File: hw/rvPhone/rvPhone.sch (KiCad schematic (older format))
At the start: 119 parts, among them J1 USB_OTG, J2 BATT, J3 SJ-3571N, Q1 MMBT3906, SW1 RESET, SW2 WAKE, U1 BQ25895, U10 74HC595, U11 ICS-43434, U12 MAX98357A, U13 FT813Q, U14 FAN5333BSX, U2 TPS62293, U3 TPS630250, U4 TMUX154E, U5 E310-G002, U6 IS25LP128-JBLE, U7 74HC00, U8 74HC00, U9 74HC595, X1 SiT1533, Y1 16MHz, Y2 12MHz

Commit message: stereo audio out; lvds display; LSM9DS1 added
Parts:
- removed BZ1: Buzzer, footprints:Buzzer_12x9.5RM5.0, symbol Device:Buzzer
- removed C38, C39: 18pF, Capacitor_SMD:C_0603_1608Metric, symbol Device:C_Small
- removed C40, C41, C43, C45, C47: 0.1uF, Capacitor_SMD:C_0603_1608Metric, symbol Device:C_Small
- removed C42, C44: 27pF, Capacitor_SMD:C_0603_1608Metric, symbol Device:C_Small
- removed C46: 4.7uF, Capacitor_SMD:C_0603_1608Metric, symbol Device:C_Small
- removed C48, C49: 1uF, Capacitor_SMD:C_0603_1608Metric, symbol Device:C
- removed C50: 10uF, Capacitor_SMD:C_0603_1608Metric, symbol Device:C
- removed C51, C53: 27pF, Capacitor_SMD:C_0603_1608Metric, symbol Device:C
- removed C52, C54: 0.1uF, Capacitor_SMD:C_0603_1608Metric, symbol Device:C
- removed D2: MBR0540, Diode_SMD:D_SOD-123, symbol Device:D_Schottky
- removed D3: 3SMAJ5935B-TP, Diode_SMD:D_SMA, symbol Device:D_Zener
- removed J3: SJ-3571N, footprints:CUI_SJ-3571N, symbol cui-sj:SJ-3571N
- removed L4: 10uH, footprints:L_Murata_LQH66SN, symbol Device:L
- removed Q1: MMBT3906, Package_TO_SOT_SMD:SOT-23, symbol Transistor_BJT:MMBT3906
- removed R28, R29: 47K, Resistor_SMD:R_0603_1608Metric, symbol Device:R
- removed U1: BQ25895, Package_DFN_QFN:Texas_S-PWQFN-N24_EP2.7x2.7mm_ThermalVias, symbol texas-tps:BQ25895
- removed U11: ICS-43434, footprints:TDK_ICS-43434, symbol ics-43434:ICS-43434
- removed U12: MAX98357A, footprints:TQFN-16-1EP_3x3mm_P0.5mm_EP1.23x1.23mm_ThermalVias, symbol max98357:MAX98357
- removed U13: FT813Q, Package_DFN_QFN:QFN-56-1EP_8x8mm_P0.5mm_EP5.6x5.6mm_ThermalVias, symbol ft81x:FT813Q
- removed U14: FAN5333BSX, Package_TO_SOT_SMD:SOT-23-5, symbol fan5333:FAN5333
- removed U2: TPS62293, footprints:TPS62290, symbol texas-tps:TPS62290
- removed U3: TPS630250, footprints:TPS630250, symbol texas-tps:TPS630250
- removed U4: TMUX154E, Package_DFN_QFN:UQFN-10_1.3x1.8mm_P0.4mm, symbol tmux:TMUX154E
- removed U5: E310-G002, Package_DFN_QFN:QFN-48-1EP_6x6mm_P0.4mm_EP4.2x4.2mm_ThermalVias, symbol e310-g000:E310-G002
- removed U6: IS25LP128-JBLE, Package_SO:SOIJ-8_5.3x5.3mm_P1.27mm, symbol is25lp128:IS25LP128
- removed X1: SiT1533, footprints:SiT1533, symbol sit1533:SiT1533
- removed Y2: 12MHz, footprints:TXC_7M, symbol Device:Crystal_GND3_Small
- added C38, C39: 10uF, Capacitor_SMD:C_0603_1608Metric, symbol Device:C
- added C40, C41: 0.1uF, Capacitor_SMD:C_0603_1608Metric, symbol Device:C
- added J3: SJ-3571N, footprints:SJ-3571N, symbol cui:SJ-3571N
- added LS2: Speaker, Connector_PinHeader_1.27mm:PinHeader_1x02_P1.27mm_Vertical, symbol Device:Speaker
- added U1: BQ25895, Package_DFN_QFN:Texas_S-PWQFN-N24_EP2.7x2.7mm_ThermalVias, symbol bq:BQ25895
- added U11: ICS-43434, footprints:ICS-43434, symbol ics:ICS-43434
- added U12, U13: MAX98357A, footprints:TQFN-16-1EP_3x3mm_P0.5mm_EP1.23x1.23mm_ThermalVias, symbol max:MAX98357
- added U14: SN74LVC1G04DRY, footprints:USON-6_1.45x1mm_P0.5mm, symbol sn74:SN74LVC1G04DRY
- added U15: SN74LVC1G3157DRY, footprints:USON-6_1.45x1mm_P0.5mm, symbol sn74:SN74LVC1G3157DRY
- added U2: TPS62293, footprints:TPS62290, symbol tps:TPS62293
- added U3: TPS630250, footprints:TPS630250, symbol tps:TPS630250
- added U4: E310-G002, Package_DFN_QFN:QFN-48-1EP_6x6mm_P0.4mm_EP4.2x4.2mm_ThermalVias, symbol sifive:E310-G002
- added U5: IS25LP128-JKLE, Package_SON:WSON-8-1EP_6x5mm_P1.27mm_EP3.4x4mm, symbol issi:IS25LP128-JKLE
- added U6: TMUX1574RSV, footprints:UQFN-16_1.8x2.6mm_P0.4mm, symbol tmux:TMUX1574RSV
- added X1: SiT1533, footprints:SiT1533, symbol sit:SiT1533
- C36: value 220pF -> 0.1uF
- C37: value 220pF -> 10uF
- R15, R16: value 1K -> 100K
- R23: value 47K -> 2K
- R24: value 22R -> 210K
- R25: value 15R -> 47K
- R26: value R -> 47K
- R27: value 47K -> 100K
- renumbered C16 to C15, C17 to C16, C18 to C17, C19 to C18, C20 to C19, C21 to C20, C22 to C21, C23 to C22, C25 to C23, C26 to C24, C27 to C25, C28 to C26, C24 to C27, C15 to C28, C35 to C34, C34 to C35, R5 to R13, R6 to R14, R13 to R28, R14 to R29, R8 to R5, R9 to R6, R35 to R8, R36 to R9
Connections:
- net BL_PWM is gone; now on net SPK_EN: R23.2
- net SPK_VO+ is gone; now on net +VSYS: C37.1
- net +1V8: now also U2.3 (FB), U4.30 (VDD), U4.46 (VDD), U4.6 (VDD)
- net +3V3: now also R27.2, C40.1, U11.5 (VDD), U14.6 (VCC), U3.12 (VOUT), U3.13 (VOUT), U3.14 (VOUT), U4.11 (IVDD), U4.12 (OTP_AIVDD), U4.19 (AON_IVDD), U4.23 (AON_VDD), U4.32 (IVDD), U4.47 (IVDD), U5.8 (VCC), U6.14 (VCC), X1.4 (VCC); no longer C34.1, C35.1, R27.1, R28.1
- net +VSYS: now also C34.1, C35.1, C36.1, R28.1, C41.1, U1.15 (SYS), U1.16 (SYS), U12.7 (VDD), U12.8 (VDD), U13.7 (VDD), U13.8 (VDD), U15.5 (VCC), U2.4 (EN), U2.5 (VIN), U3.4 (VIN), U3.5 (VIN), U3.6 (VIN), U3.7 (VINA), U3.8 (EN); no longer R23.1
- net ESP32.IO39: now also U1.7 (INT)
- net GND: now also R15.2, Y1.3, C40.2, C41.2, J3.1, U1.17 (PGND), U1.18 (PGND), U1.25 (EP), U1.8 (OTG), U1.9 (/CE), U11.2 (LR), U11.3 (GND), U12.11 (GND), U12.15 (GND), U12.17 (EP), U12.3 (GND), U13.11 (GND), U13.15 (GND), U13.17 (EP), U13.3 (GND), U14.3 (GND), U15.2 (GND), U2.2 (MODE), U2.6 (GND), U2.7 (EP), U3.10 (PFM), U3.2 (PGND), U3.9 (GND), U4.21 (AON_PSD_LFCLKSEL), U4.49 (GND), U5.4 (VSS), U5.9 (EP), U6.13 (/EN), U6.6 (GND), X1.2 (GND); no longer R24.2, U8.12, U8.13
- net GPIO_0: now also U4.25 (GPIO_0/PWM0.0)
- net GPIO_12: now also U4.36 (GPIO_12/PWM2.2), U6.7 (D3)
- net GPIO_13: now also U4.37 (GPIO_13/PWM2.3), U6.5 (D2)
- net GPIO_18: now also U4.40 (GPIO_18)
- net GPIO_20: now also U4.42 (GPIO_20/PWM1.0)
- net GPIO_22: now also U4.44 (GPIO_22/PWM1.3)
- net GPIO_23: now also U4.45 (GPIO_23)
- net JTAG_TCK: now also U4.13 (JTAG_TCK)
- net JTAG_TDI: now also U4.16 (JTAG_TDI)
- net JTAG_TDO: now also U4.14 (JTAG_TDO)
- net JTAG_TMS: now also U4.15 (JTAG_TMS)
- net PLL_AVDD: now also U4.7 (PLL_AVDD)
- net PLL_AVSS: now also U4.8 (PLL_AVSS)
- net PSD_LFALTCLK: now also U4.20 (AON_PSD_LFALTCLK), X1.3 (CLKOUT)
- net PWM0.1: now also U4.26 (GPIO_1/PWM0.1), U6.10 (D4); no longer R18.2, U7.1, U8.1, U8.2
- net PWM1.1: now also U4.41 (GPIO_19/PWM1.1), U6.2 (D1); no longer R19.2
- net PWM1.2: now also U4.43 (GPIO_21/PWM1.2)
- net PWM2.1: now also U8.1, U12.14 (LRCLK), U13.14 (LRCLK), U4.35 (GPIO_11/PWM2.1); no longer U8.10
- net QSPI_CLK: now also U4.48 (QSPI_CLK), U5.6 (SCK)
- net QSPI_CS: now also U4.5 (QSPI_CS), U5.1 (S#)
- net QSPI_DQ_0: now also U4.4 (QSPI_DQ_0), U5.5 (MOSI/IO0)
- net QSPI_DQ_1: now also U4.3 (QSPI_DQ_1), U5.2 (MISO/IO1)
- net QSPI_DQ_2: now also U4.2 (QSPI_DQ_2), U5.3 (WP#/IO2)
- net QSPI_DQ_3: now also U4.1 (QSPI_DQ_3), U5.7 (HOLD#/IO3)
- net RESET: now also U4.24 (AON_ERST_N)
- net SPI1.MISO: now also U4.29 (GPIO_4/SPI1.MISO)
- net SPI1.MOSI: now also U4.28 (GPIO_3/SPI1.MOSI/PWM0.3)
- net SPI1.SCK: now also U4.31 (GPIO_5/SPI1.SCK)
- net SPI1.SS0: now also U4.27 (GPIO_2/SPI1.SS0/PWM0.2)
- net SPI1.SS2: now also U4.33 (GPIO_9/SPI1.SS2); no longer R27.2
- net SPI1.SS3: now also U4.34 (GPIO_10/SPI1.SS3/PWM2.0)
- net SPK_CLK: now also U8.11, U12.16 (BCLK), U13.16 (BCLK); no longer U8.3
- net SPK_EN: now also R24.2, U6.15 (SEL)
- net SPK_GAIN: now also U12.2 (GAIN_SLOT), U13.2 (GAIN_SLOT), U15.4 (A)
- net TMUX.I2C0.SCL: now also U1.5 (SCL), U6.3 (S2A)
- net TMUX.I2C0.SDA: now also U1.6 (SDA), U6.9 (S3A)
- net UART0.RX: now also U4.38 (GPIO_16/UART0.RX)
- net UART0.TX: now also U4.39 (GPIO_17/UART0.TX)
- net VBUS: now also U1.1 (VBUS)
- net WAKE: now also U1.12 (/QON), U4.18 (AON_PMU_DWAKEUP_N)
- net XTAL_XI: now also U4.9 (16M_XTAL_XI)
- net XTAL_XO: now also U4.10 (16M_XTAL_XO)
- net at L2.1: now also U2.1 (SW)
- net TMUX.GPIO0: now reaches R15.1
- net TMUX.GPIO0: now also U6.16 (S1A)
- net SPK_GAIN_SEL: now reaches U8.8
- net SPK_GAIN_SEL: now also U15.6 (S); no longer R15.2
- net TMUX.GPIO1: now reaches R16.1
- net TMUX.GPIO1: now also U6.12 (S4A)
- net at R1.1: now also U1.10 (ILIM)
- net at R2.2, R4.1: now also U1.11 (TS)
- net at C6.1, J2.1 (Pin_1): now also U1.13 (BAT), U1.14 (BAT)
- net at C1.1, L1.1: now also U1.19 (SW), U1.20 (SW)
- net at J1.3 (D+): now also U1.2 (D+)
- net at C1.2: now also U1.21 (BTST)
- net at C5.1, R2.1: now also U1.22 (REGN)
- net at C55.1, C56.1: now also U1.23 (PMID)
- net at J1.2 (D-): now also U1.3 (D-)
- net at R3.1: now also U1.4 (STAT)
- net at L3.1: now also U3.3 (L1)
- net at L3.2: now also U3.1 (L2)
- net at R29.1: now also U15.3 (B1)
- net at R28.2: now also U15.1 (B2)
- net at R5.2, R6.1: now also U3.11 (FB)
- net at U8.6: now also U8.2; no longer U8.9
- removed net DISP_LED_K: R24.1, R25.1, R26.1
- net EAR_VO+ renamed SPK_L+
- net SPK_L+: now also J3.4
- net I2S_SD_IN renamed SPK_SD
- net SPK_SD: now also U12.1 (DIN), U13.1 (DIN), U6.4 (S2B)
- net I2S_SD_OUT renamed MIC_SD
- net MIC_SD: now also U11.6 (SD), U6.8 (S3B)
- net SPK_VO- renamed SPK_L-
- net SPK_L-: now also U12.10 (OUTN); no longer C36.1
- new net: R23.1, U12.4 (SD_MODE)
- new net: R24.1, U13.4 (SD_MODE)
- new net: C39.1, J3.2, R26.1
- new net: C39.2, J3.6
- new net: C38.1, J3.3, R25.1
- new net: C38.2, J3.9
- new net BT81X.GPIO2: U8.10
- new net DISP_CS: U8.3
- new net HP_DET: J3.10, J3.11, R27.1, U14.2 (A)
- new net HP_SWITCH: U14.4 (Y), U8.9
- new net MIC_CLK: R18.2, U11.4 (SCK), U6.11 (S4B), U7.1, U8.12, U8.13
- new net MIC_WS: R19.2, U11.1 (WS), U6.1 (S1B)
- new net SPK_L_HP+: J3.5, U12.9 (OUTP)
- new net SPK_R+: J3.7, LS2.1
- new net SPK_R-: LS2.2, U13.10 (OUTN)
- new net SPK_R_HP_+: J3.8, U13.9 (OUTP)
- no-connect marks 26 -> 21
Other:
- moved on the sheet: C1, C10, C11, C12, C13, C14, C15, C16, C17, C18, C19, C2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

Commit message: rev2 board
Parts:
- removed LS1, LS2: Speaker, Connector_PinHeader_1.27mm:PinHeader_1x02_P1.27mm_Vertical, symbol Device:Speaker
- removed U14: SN74LVC1G04DRY, footprints:USON-6_1.45x1mm_P0.5mm, symbol sn74:SN74LVC1G04DRY
- removed U15: SN74LVC1G3157DRY, footprints:USON-6_1.45x1mm_P0.5mm, symbol sn74:SN74LVC1G3157DRY
- removed U4: E310-G002, Package_DFN_QFN:QFN-48-1EP_6x6mm_P0.4mm_EP4.2x4.2mm_ThermalVias, symbol sifive:E310-G002
- added C42: 10uF, Capacitor_SMD:C_0603_1608Metric, symbol Device:C
- added C45: 0.1uF, Capacitor_SMD:C_0603_1608Metric, symbol Device:C_Small
- added J3: +5V, Connector_PinHeader_2.54mm:PinHeader_1x02_P2.54mm_Vertical, symbol Connector_Generic:Conn_01x02
- added J5: SPEAKER, Connector_PinHeader_2.54mm:PinHeader_1x04_P2.54mm_Vertical, symbol Connector_Generic:Conn_01x04
- added TP1: BQ_INT, TestPoint:TestPoint_Pad_D1.5mm, symbol Connector:TestPoint
- added U14: SN74LVC1G04DCK, footprints:Texas_R-PDSO-G5, symbol sn74:SN74LVC1G04DCK
- added U15: SN74LVC1G3157DCK, Package_TO_SOT_SMD:Texas_R-PDSO-G6, symbol sn74:SN74LVC1G3157DCK
- added U16: SN74LVC2G07DCK, Package_TO_SOT_SMD:Texas_R-PDSO-G6, symbol sn74:SN74LVC2G07DCK
- added U4: FE310-G002, Package_DFN_QFN:QFN-48-1EP_6x6mm_P0.4mm_EP4.2x4.2mm_ThermalVias, symbol sifive:FE310-G002
- C10: value 22uF -> 10uF
- C11: value 22uF -> 47uF; footprint Capacitor_SMD:C_0603_1608Metric -> Capacitor_SMD:C_0805_2012Metric
- C25, C26: value 12pF -> 10pF
- C43: renamed from C55; footprint Capacitor_SMD:C_0603_1608Metric -> Capacitor_SMD:C_0805_2012Metric
- C44: renamed from C56; footprint Capacitor_SMD:C_0603_1608Metric -> Capacitor_SMD:C_0805_2012Metric
- J2: footprint Connector_PinHeader_2.00mm:PinHeader_1x02_P2.00mm_Vertical -> Connector_PinHeader_2.54mm:PinHeader_1x02_P2.54mm_Vertical
- L1: footprint footprints:L_Coilcraft_LPS3015 -> Inductor_SMD:L_Vishay_IHLP-1616
- R23: value 2K -> 2.2K
- R24: value 210K -> 255K
- R28, R29: value 100K -> 50K
- R7: value 10K -> 100K
- SW1: footprint footprints:Panasonic_EVPBB -> Button_Switch_SMD:SW_SPST_PTS810
- SW2: footprint footprints:Panasonic_EVPAK -> footprints:Panasonic_EVPAE
- renumbered J3 to J4
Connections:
- net +1V8: now also U4.30 (VDD), U4.46 (VDD), U4.6 (VDD)
- net +3V3: now also C45.1, U14.5 (VCC), U16.5 (VCC), U4.11 (IVDD), U4.12 (OTP_AIVDD), U4.19 (AON_IVDD), U4.23 (AON_VDD), U4.32 (IVDD), U4.47 (IVDD)
- net +VSYS: now also U1.8 (OTG), U15.5 (VCC)
- net GND: now also J1.6 (Shield), C42.2, C45.2, J3.2 (Pin_2), U14.3 (GND), U15.2 (GND), U16.2 (GND), U4.21 (AON_PSD_LFCLKSEL), U4.49 (GND); no longer U1.8 (OTG)
- net GPIO_0: now also U4.25 (GPIO_0/PWM0.0)
- net GPIO_12: now also U4.36 (GPIO_12/PWM2.2)
- net GPIO_13: now also U4.37 (GPIO_13/PWM2.3)
- net GPIO_18: now also U7.12, U7.13, U4.40 (GPIO_18); no longer U7.10, U7.9
- net GPIO_20: now also U4.42 (GPIO_20/PWM1.0)
- net GPIO_22: now also U4.44 (GPIO_22/PWM1.3)
- net GPIO_23: now also U4.45 (GPIO_23)
- net HP_DET: now also U14.2 (A)
- net HP_SWITCH: now also U14.4 (Y)
- net JTAG_TCK: now also U4.13 (JTAG_TCK)
- net JTAG_TDI: now also U4.16 (JTAG_TDI)
- net JTAG_TDO: now also U4.14 (JTAG_TDO)
- net JTAG_TMS: now also U4.15 (JTAG_TMS)
- net PLL_AVDD: now also U4.7 (PLL_AVDD)
- net PLL_AVSS: now also U4.8 (PLL_AVSS)
- net PSD_LFALTCLK: now also U4.20 (AON_PSD_LFALTCLK)
- net PWM0.1: now also U4.26 (GPIO_1/PWM0.1)
- net PWM1.1: now also U4.41 (GPIO_19/PWM1.1)
- net PWM1.2: now also U7.9, U4.43 (GPIO_21/PWM1.2); no longer U7.13
- net PWM2.1: now also U4.35 (GPIO_11/PWM2.1)
- net QSPI_CLK: now also U4.48 (QSPI_CLK)
- net QSPI_CS: now also U4.5 (QSPI_CS)
- net QSPI_DQ_0: now also U4.4 (QSPI_DQ_0)
- net QSPI_DQ_1: now also U4.3 (QSPI_DQ_1)
- net QSPI_DQ_2: now also U4.2 (QSPI_DQ_2)
- net QSPI_DQ_3: now also U4.1 (QSPI_DQ_3)
- net RESET: now also U16.6 (1Y), U4.24 (AON_ERST_N)
- net SPI1.MISO: now also U4.29 (GPIO_4/SPI1.MISO)
- net SPI1.MOSI: now also U4.28 (GPIO_3/SPI1.MOSI/PWM0.3)
- net SPI1.SCK: now also U4.31 (GPIO_5/SPI1.SCK)
- net SPI1.SS0: now also U4.27 (GPIO_2/SPI1.SS0/PWM0.2)
- net SPI1.SS2: now also U4.33 (GPIO_9/SPI1.SS2)
- net SPI1.SS3: now also U4.34 (GPIO_10/SPI1.SS3/PWM2.0)
- net SPK_EN: now also U7.8; no longer U7.11
- net SPK_GAIN: now also U15.4 (A)
- net SPK_GAIN_SEL: now also U15.6 (S)
- net SPK_L+: now also J5.1 (Pin_1)
- net SPK_L-: now also J5.2 (Pin_2)
- net SPK_R+: now also J5.3 (Pin_3)
- net SPK_R-: now also J5.4 (Pin_4)
- net VBUS: now also C42.1
- net WAKE: now also U16.3 (2A), U4.18 (AON_PMU_DWAKEUP_N); no longer U1.12 (/QON)
- net XTAL_XI: now also U4.9 (16M_XTAL_XI)
- net XTAL_XO: now also U4.10 (16M_XTAL_XO)
- net at R28.2: now also U15.1 (B2)
- net at R29.1: now also U15.3 (B1)
- net at U1.3 (D-): now also U1.2 (D+); no longer J1.2 (D-)
- net USB_D+: now reaches J1.3 (D+)
- net USB_D+: no longer U1.2 (D+)
- net BQ_PMID: now reaches C43.1, C44.1, U1.23 (PMID)
- net BQ_PMID: now also J3.1 (Pin_1)
- net ESP32.IO39 renamed BQ_INT
- net BQ_INT: now also TP1.1; no longer R7.2
- new net: U7.10, U7.11
- new net BQ_QON: U1.12 (/QON), U16.4 (2Y)
- new net JTAG_TRST_N: R7.2, U16.1 (1A)
- new net UART0.RXD: U4.38 (GPIO_16/UART0.RX)
- new net UART0.TXD: U4.39 (GPIO_17/UART0.TX)
- new net USB_D-: J1.2 (D-)
- no-connect marks 21 -> 20
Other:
- moved on the sheet: C1, C10, C11, C12, C13, C14, C15, C16, C17, C18, C19, C2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

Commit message: temp commit for merge
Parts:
- removed C14: 10nF, Capacitor_SMD:C_0603_1608Metric, symbol Device:C_Small
- added C14: 22uF, Capacitor_SMD:C_0805_2012Metric, symbol Device:C
- added R23, R24, R25, R31: 100K, Resistor_SMD:R_0603_1608Metric, symbol Device:R
- added TP2: PMU_OUT0, TestPoint:TestPoint_Pad_D1.5mm, symbol Connector:TestPoint
- J1: footprint footprints:USB_Micro-B -> footprints:GCT_MicroUSB-USB3080
- L2: footprint footprints:L_Coilcraft_LPS3015 -> footprints:Coilcraft-LPS3015
- L3: footprint footprints:L_Coilcraft_XAL40 -> footprints:Coilcraft-XAL40
- U10, U9: footprint footprints:74HC595BQ115 -> footprints:DHVQFN-16_2.5x3.5mm_P0.5mm_EP1.0x2.0mm; symbol 74xx:74HC595 -> 74xx-ep:74HC595
- U7, U8: footprint footprints:74HC00BQ115 -> footprints:DHVQFN-14_2.5x3.0mm_P0.5mm_EP1.0x1.5mm; symbol 74xx:74HC00 -> 74xx-ep:74HC00
- renumbered R23 to R26, R24 to R27, R25 to R28, R26 to R29, R27 to R30, R28 to R32, R29 to R33
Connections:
- net labels added: AON_PMU_OUT_0, AON_PMU_OUT_1
- wire segments 597 -> 622
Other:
- moved on the sheet: C12, C13, C15, C16, C17, C18, C19, C20, C21, C22, C23, C24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

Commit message: HW REV 3.0
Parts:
- removed R26: 2.2K, Resistor_SMD:R_0603_1608Metric, symbol Device:R
- removed TP1: BQ_INT, TestPoint:TestPoint_Pad_D1.5mm, symbol Connector:TestPoint
- removed U15: SN74LVC1G3157DCK, Package_TO_SOT_SMD:Texas_R-PDSO-G6, symbol sn74:SN74LVC1G3157DCK
- added C39, C40, C45: 0.1uF, Capacitor_SMD:C_0603_1608Metric, symbol Device:C
- added C53, C54, C7: 10uF, Capacitor_SMD:C_0603_1608Metric, symbol Device:C
- added D1: B5817WS, footprints:D_SOD-323, symbol Device:D_Schottky
- added J6: Ext Audio, Connector_Molex:Molex_SlimStack_54722-0164_2x08_P0.50mm_Vertical, symbol Connector_Generic:Conn_02x08_Odd_Even
- added JP1: AUDIO PWR, Jumper:SolderJumper-3_P1.3mm_Open_RoundedPad1.0x1.5mm, symbol Jumper:SolderJumper_3_Open
- added U15, U16: MAX14689A, footprints:TDFN-10-1EP_2x2.5mm_P0.4mm_EP1.3x1.4mm_ThermalVias, symbol max:MAX14689A
- added U18: TMUX1119DCK, Package_TO_SOT_SMD:Texas_R-PDSO-G6, symbol tmux:TMUX1119DCK
- added U19: 74LVC1G02, footprints:Texas_R-PDSO-G5, symbol 74xGxx:74LVC1G02
- L1: footprint Inductor_SMD:L_Vishay_IHLP-1616 -> Inductor_SMD:L_Vishay_IHLP-2525
- R2: value 10K -> 5.23K
- R27: value 255K -> 210K
- R3: renamed from R4; value 10K -> 30.1K
- renumbered C4 to C1, C9 to C10, C10 to C11, C11 to C12, C12 to C13, C13 to C14, C1 to C2, C45 to C28, C28 to C29, C5 to C3, C29 to C30, C30 to C31, C31 to C32, C32 to C33, C33 to C34, C34 to C35, C35 to C36, C36 to C37, C37 to C38, C2 to C4, C38 to C41, C39 to C42, C40 to C43, C41 to C44, C3 to C5, C42 to C50, C43 to C51, C44 to C52, C14 to C55, C7 to C8, C8 to C9, D1 to D2, R16 to R15, R15 to R16, R31 to R26, R32 to R31, R33 to R32, R3 to R4, U9 to U10, U10 to U11, U11 to U12, U12 to U13, U13 to U14, U14 to U17, U16 to U6, U6 to U7, U7 to U8, U8 to U9
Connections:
- net labels added: AUDIO_OUT_L+, AUDIO_OUT_L-, AUDIO_OUT_R+, AUDIO_OUT_R-, BQ.INT, BQ_SW, BT81X.AUDIO, EXT_AUDIO_EN, HP_L, HP_R, VDDA, ~HP_DET
- net labels removed: BQ_INT, HP_SWITCH, SPK_L_HP+, SPK_R_HP_+
- wire segments 622 -> 705
- no-connect marks 20 -> 32
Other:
- moved on the sheet: C1, C10, C11, C12, C13, C14, C15, C16, C17, C18, C19, C20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

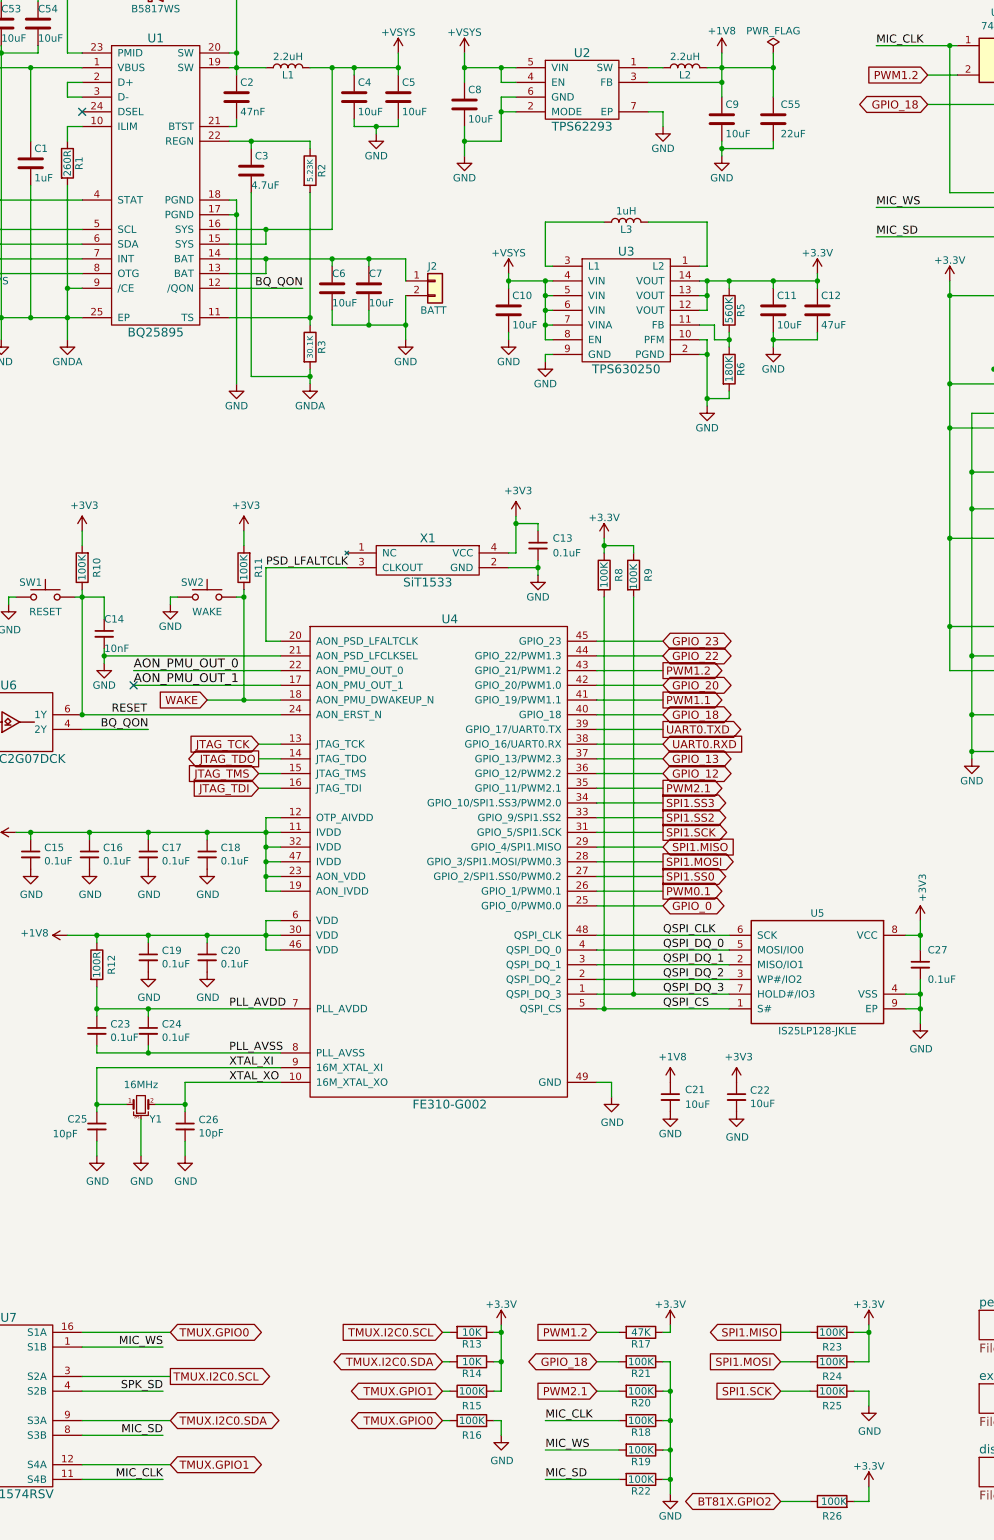
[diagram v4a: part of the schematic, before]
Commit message: added pull-up pull-dn resistors; fixed input power;
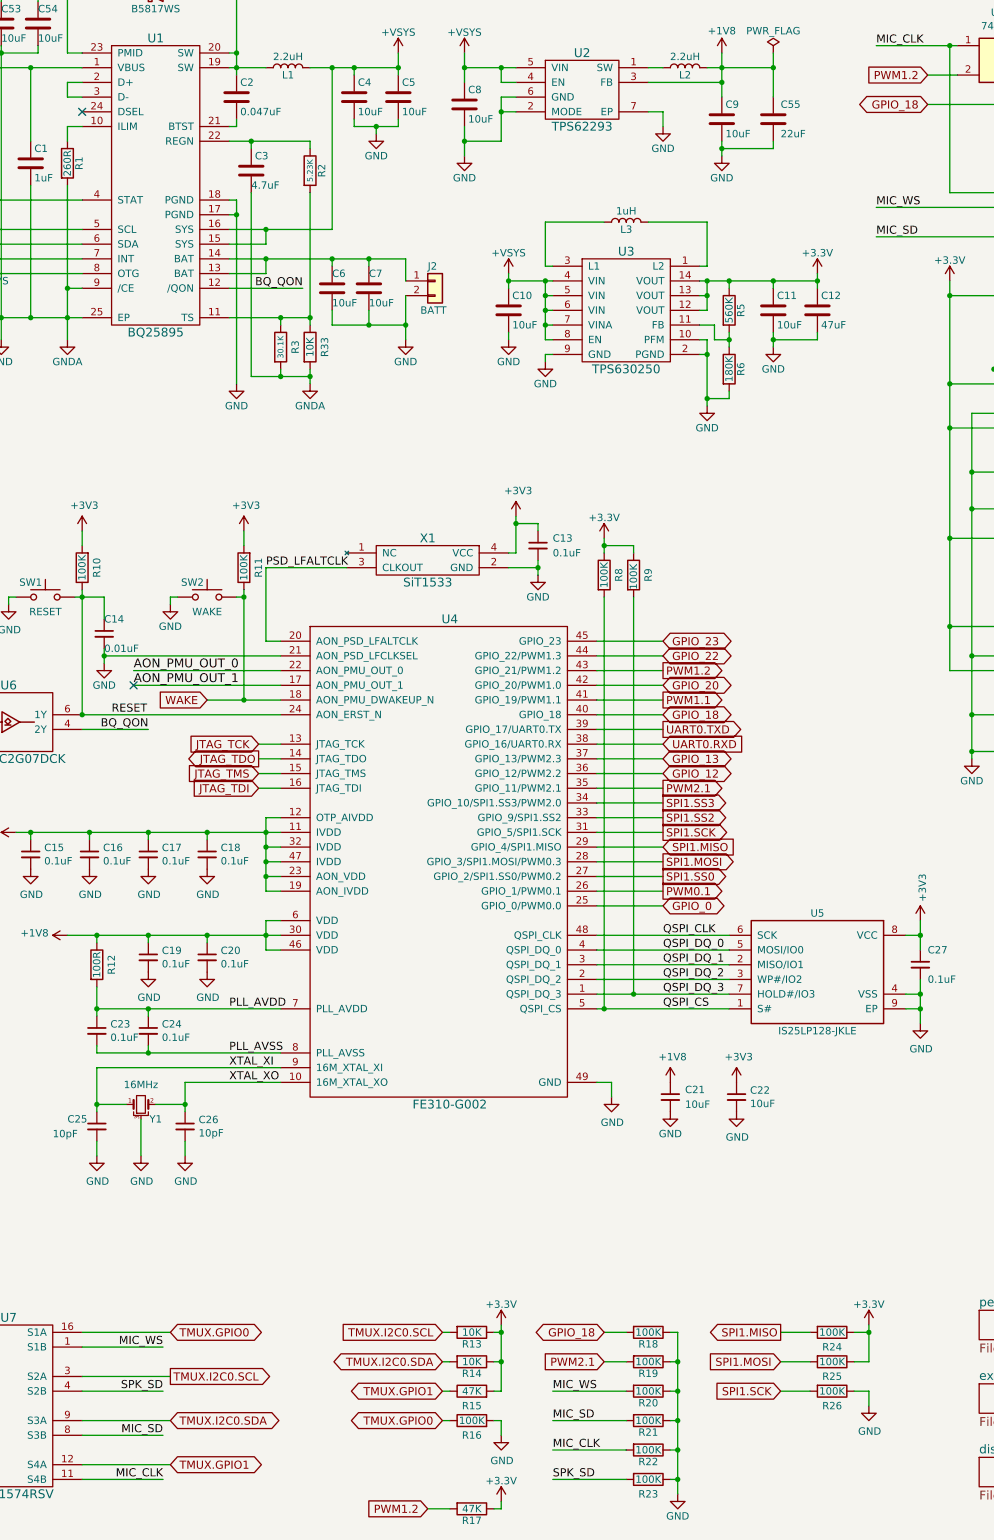
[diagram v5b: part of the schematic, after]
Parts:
- removed R26: 100K, Resistor_SMD:R_0603_1608Metric, symbol Device:R
- added R23: 100K, Resistor_SMD:R_0603_1608Metric, symbol Device:R
- added R33: 10K, Resistor_SMD:R_0603_1608Metric, symbol Device:R
- C14: value 10nF -> 0.01uF
- C2: value 47nF -> 0.047uF
- R15: value 100K -> 47K
- renumbered R21 to R18, R20 to R19, R19 to R20, R22 to R21, R18 to R22, R23 to R24, R24 to R25, R25 to R26
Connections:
- wire segments 705 -> 709
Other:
- moved on the sheet: R17, R18, R19, R20, R21, R22, R3

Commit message: REV3.1:  - fixed audio  - added spacers  - UART is routed through audio mux instead of I2C  - proper display connector alignment
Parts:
- removed J4: SJ-3571N, footprints:SJ-3571N, symbol cui:SJ-3571N
- added C46: 0.1uF, Capacitor_SMD:C_0603_1608Metric, symbol Device:C
- added J4: AudioJack, footprints:35RASMT4BHNTRX, symbol Connector:AudioJack3_SwitchTR
- added R34, R35: 100K, Resistor_SMD:R_0603_1608Metric, symbol Device:R
- added U20: SN74LVC2G66DCU, Package_SO:VSSOP-8_2.3x2mm_P0.5mm, symbol sn74:SN74LVC2G66DCU
- R16: renamed from R15; value 47K -> 100K
- R32: value 50K -> 0R
- renumbered R16 to R15, R23 to R18, R18 to R19, R19 to R20, R20 to R21, R21 to R22, R22 to R23
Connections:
- net labels added: +5V, BT81X.INT, CTP.RST, GPIO_16, GPIO_17, I2C0.SCL, I2C0.SDA, SD_IN, SD_OUT
- net labels removed: BQ_PMID, GPIO_12, GPIO_13, TMUX.GPIO0, TMUX.GPIO1, TMUX.I2C0.SCL, TMUX.I2C0.SDA
- wire segments 709 -> 731
- no-connect marks 32 -> 26
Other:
- moved on the sheet: C1, C10, C11, C12, C2, C21, C22, C25, C26, C27, C29, C3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
